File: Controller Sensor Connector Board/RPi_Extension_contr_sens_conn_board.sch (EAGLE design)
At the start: 39 parts, among them J1 22-27-2051-05, J2 22-27-2051-05, X17 53047-03, X18 53047-03, X19 53047-03, X20 53047-03, X21 53047-03, X22 53047-03, X23 53047-03, X24 53047-03, X25 53047-03, X26 53047-03, X27 53047-03, X28 53047-03, X29 53047-03, X30 53047-03, X31 53047-03, X32 53047-03

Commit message: added 40pin connector using 3pin 2row for each muscle
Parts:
- added SV10, SV11, SV12, SV13, SV14, SV15, SV16, SV6, SV7, SV8, SV9: (no value), con-lstb:MA03-2
- added U1: 5103309-8, AMP 5103309-8 40pin:5103309-8
- SV1, SV2, SV3, SV4: device con-lstb:MA08-2 -> con-lstb:MA03-2
- SV5: device con-lstb:MA20-2 -> con-lstb:MA03-2
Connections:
- removed net N$43: X30-1.S
- new net ADC_1: SV1.3
- new net ADC_10: SV10.3
- new net ADC_11: SV11.3
- new net ADC_12: SV12.3
- new net ADC_13: SV13.3
- new net ADC_14: SV14.3
- new net ADC_15: SV15.3
- new net ADC_16: SV16.3
- new net ADC_2: SV2.3
- new net ADC_3: SV3.3
- new net ADC_4: SV4.3
- new net ADC_5: SV5.3
- new net ADC_6: SV6.3
- new net ADC_7: SV7.3
- new net ADC_8: SV8.3
- new net ADC_9: SV9.3, X30-1.S
- new net DAC_1: SV1.1, U1.40
- new net DAC_10: SV10.1, U1.34
- new net DAC_11: SV11.1, U1.30
- new net DAC_12: SV12.1, U1.26
- new net DAC_13: SV13.1, U1.22
- new net DAC_14: SV14.1, U1.18
- new net DAC_15: SV15.1, U1.14
- new net DAC_16: SV16.1, U1.10
- new net DAC_2: SV2.1, U1.36
- new net DAC_3: SV3.1, U1.32
- new net DAC_4: SV4.1, U1.28
- new net DAC_5: SV5.1, U1.24
- new net DAC_6: SV6.1, U1.20
- new net DAC_7: SV7.1, U1.16
- new net DAC_8: SV8.1, U1.12
- new net DAC_9: SV9.1, U1.38
- new net N$100: X1.5
- new net N$101: X5.3
- new net N$102: X5.5
- new net N$103: X9.5
- new net N$104: X9.3
- new net N$105: X2.5
- new net N$106: X2.3
- new net N$107: X6.5
- new net N$108: X6.3
- new net N$109: X10.5
- new net N$11: X11.3
- new net N$110: X10.3
- new net N$111: X16.5
- new net N$112: X16.3
- new net N$12: X11.5
- new net N$14: X7.3
- new net N$15: X7.5
- new net N$17: X3.3
- new net N$18: X3.5
- new net N$2: X13.5
- new net N$20: X4.3
- new net N$21: X4.5
- new net N$23: X8.5
- new net N$24: X8.3
- new net N$26: X12.5
- new net N$27: X12.3
- new net N$3: X13.3
- new net N$5: X14.5
- new net N$6: X14.3
- new net N$67: SV1.6
- new net N$68: SV1.5
- new net N$69: SV5.5
- new net N$70: SV5.6
- new net N$71: SV2.6
- new net N$72: SV2.5
- new net N$73: SV6.6
- new net N$74: SV6.5
- new net N$75: SV9.6
- new net N$76: SV9.5
- new net N$77: SV13.6
- new net N$78: SV13.5
- new net N$79: SV10.6
- new net N$8: X15.3
- new net N$80: SV10.5
- new net N$81: SV14.5
- new net N$82: SV14.6
- new net N$83: SV15.5
- new net N$84: SV15.6
- new net N$85: SV16.6
- new net N$86: SV16.5
- new net N$87: SV12.5
- new net N$88: SV12.6
- new net N$89: SV11.6
- new net N$9: X15.5
- new net N$90: SV11.5
- new net N$91: SV8.5
- new net N$92: SV8.6
- new net N$93: SV4.5
- new net N$94: SV4.6
- new net N$95: SV3.5
- new net N$96: SV3.6
- new net N$97: SV7.5
- new net N$98: SV7.6
- new net N$99: X1.3
- net GND: now also SV1.2, SV1.4, SV10.2, SV10.4, SV11.2, SV11.4, SV12.2, SV12.4, SV13.2, SV13.4, SV14.2, SV14.4, SV15.2, SV15.4, SV16.2, SV16.4, SV2.2, SV2.4, SV3.2, SV3.4, SV4.2, SV4.4, SV5.2, SV5.4, SV6.2, SV6.4, SV7.2, SV7.4, SV8.2, SV8.4, SV9.2, SV9.4, U1.1, U1.11, U1.13, U1.15, U1.17, U1.19, U1.21, U1.23, U1.25, U1.27, U1.29, U1.3, U1.31, U1.33, U1.35, U1.37, U1.39, U1.5, U1.7, U1.9

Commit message: finished first half of connector board
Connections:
- net N$67 renamed LC_P_1
- net N$68 renamed LC_N_1
- removed net N$103: X9.5
- removed net N$104: X9.3
- removed net N$109: X10.5
- removed net N$11: X11.3
- removed net N$110: X10.3
- removed net N$12: X11.5
- removed net N$13: X24-1.S
- removed net N$14: X7.3
- removed net N$15: X7.5
- removed net N$16: X23-1.S
- removed net N$2: X13.5
- removed net N$23: X8.5
- removed net N$24: X8.3
- removed net N$25: X25-1.S
- removed net N$26: X12.5
- removed net N$27: X12.3
- removed net N$28: X26-1.S
- removed net N$3: X13.3
- removed net N$31: X27-1.S
- removed net N$34: X28-1.S
- removed net N$46: X29-1.S
- removed net N$5: X14.5
- removed net N$6: X14.3
- removed net N$75: SV9.6
- removed net N$76: SV9.5
- removed net N$77: SV13.6
- removed net N$78: SV13.5
- removed net N$79: SV10.6
- removed net N$80: SV10.5
- removed net N$81: SV14.5
- removed net N$82: SV14.6
- removed net N$83: SV15.5
- removed net N$84: SV15.6
- removed net N$85: SV16.6
- removed net N$86: SV16.5
- removed net N$87: SV12.5
- removed net N$88: SV12.6
- removed net N$89: SV11.6
- removed net N$90: SV11.5
- new net LC_N_10: SV10.5, X13.3
- new net LC_N_11: SV11.5, X12.3
- new net LC_N_12: SV12.5, X11.3
- new net LC_N_13: SV13.5, X10.3
- new net LC_N_14: SV14.5, X9.3
- new net LC_N_15: SV15.5, X8.3
- new net LC_N_16: SV16.5, X7.3
- new net LC_N_9: SV9.5, X14.3
- new net LC_P_10: SV10.6, X13.5
- new net LC_P_11: SV11.6, X12.5
- new net LC_P_12: SV12.6, X11.5
- new net LC_P_13: SV13.6, X10.5
- new net LC_P_14: SV14.6, X9.5
- new net LC_P_15: SV15.6, X8.5
- new net LC_P_16: SV16.6, X7.5
- new net LC_P_9: SV9.6, X14.5
- net ADC_10: now also X29-1.S
- net ADC_11: now also X28-1.S
- net ADC_12: now also X27-1.S
- net ADC_13: now also X26-1.S
- net ADC_14: now also X25-1.S
- net ADC_15: now also X24-1.S
- net ADC_16: now also X23-1.S
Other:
- moved on the sheet: SV1, SV10, SV11, SV13, SV14, SV15, SV2, SV3, SV5, SV6, SV7, SV9

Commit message: finished second half of connector board
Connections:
- removed net N$1: X17-1.S
- removed net N$10: X20-1.S
- removed net N$100: X1.5
- removed net N$101: X5.3
- removed net N$102: X5.5
- removed net N$105: X2.5
- removed net N$106: X2.3
- removed net N$107: X6.5
- removed net N$108: X6.3
- removed net N$111: X16.5
- removed net N$112: X16.3
- removed net N$17: X3.3
- removed net N$18: X3.5
- removed net N$19: X22-1.S
- removed net N$20: X4.3
- removed net N$21: X4.5
- removed net N$22: X21-1.S
- removed net N$37: X32-1.S
- removed net N$4: X18-1.S
- removed net N$40: X31-1.S
- removed net N$69: SV5.5
- removed net N$7: X19-1.S
- removed net N$70: SV5.6
- removed net N$71: SV2.6
- removed net N$72: SV2.5
- removed net N$73: SV6.6
- removed net N$74: SV6.5
- removed net N$8: X15.3
- removed net N$9: X15.5
- removed net N$91: SV8.5
- removed net N$92: SV8.6
- removed net N$93: SV4.5
- removed net N$94: SV4.6
- removed net N$95: SV3.5
- removed net N$96: SV3.6
- removed net N$97: SV7.5
- removed net N$98: SV7.6
- removed net N$99: X1.3
- new net LC_N_2: SV2.5, X16.3
- new net LC_N_3: SV3.5, X1.3
- new net LC_N_4: SV4.5, X2.3
- new net LC_N_5: SV5.5, X3.3
- new net LC_N_6: SV6.5, X4.3
- new net LC_N_7: SV7.5, X5.3
- new net LC_N_8: SV8.5, X6.3
- new net LC_P_2: SV2.6, X16.5
- new net LC_P_3: SV3.6, X1.5
- new net LC_P_4: SV4.6, X2.5
- new net LC_P_5: SV5.6, X3.5
- new net LC_P_6: SV6.6, X4.5
- new net LC_P_7: SV7.6, X5.5
- new net LC_P_8: SV8.6, X6.5
- net ADC_1: now also X31-1.S
- net ADC_2: now also X32-1.S
- net ADC_3: now also X17-1.S
- net ADC_4: now also X18-1.S
- net ADC_5: now also X19-1.S
- net ADC_6: now also X20-1.S
- net ADC_7: now also X21-1.S
- net ADC_8: now also X22-1.S
- net LC_N_1: now also X15.3
- net LC_P_1: now also X15.5
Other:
- moved on the sheet: J1-1, J1-2, J1-3, J1-4, J1-5, J2-1, J2-2, J2-3, J2-4, J2-5, SV1, SV10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

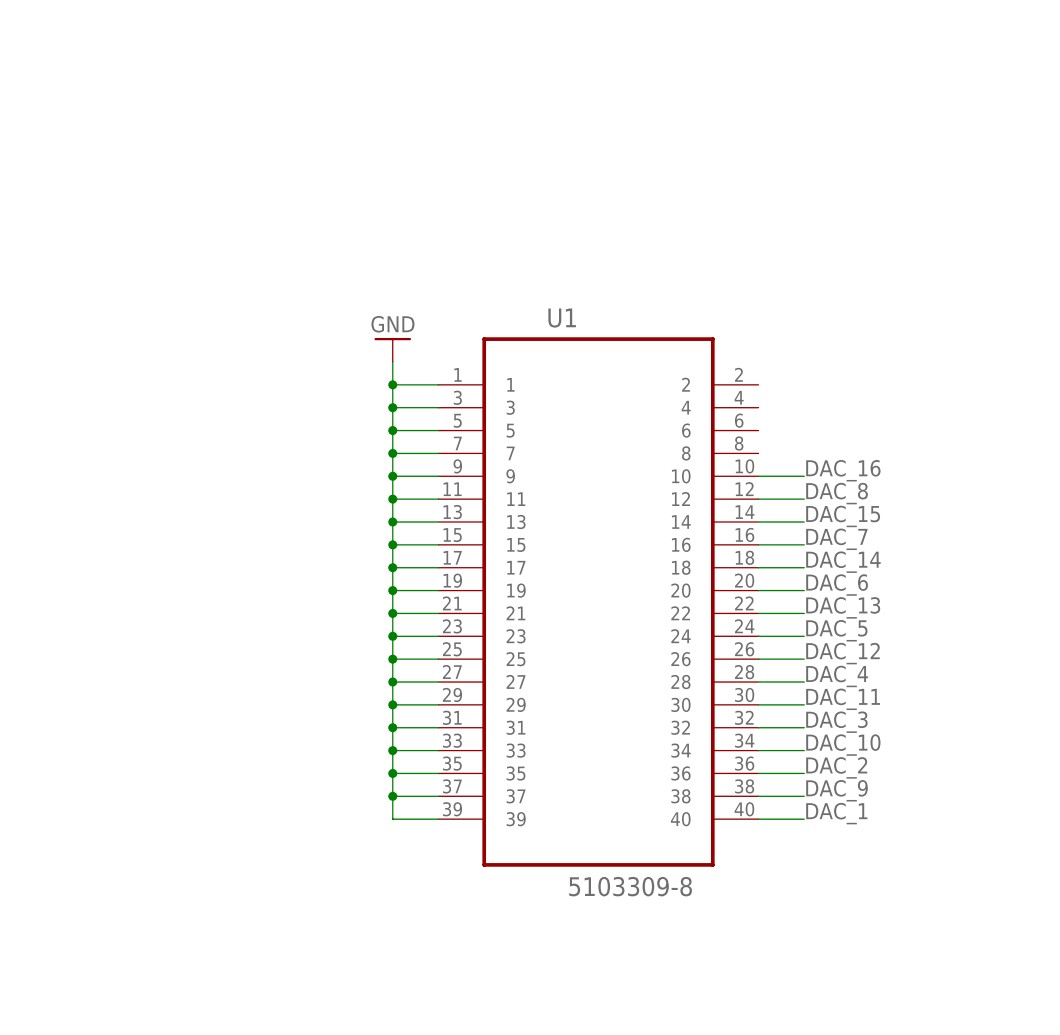
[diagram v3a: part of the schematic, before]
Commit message: adjusted silkscreen
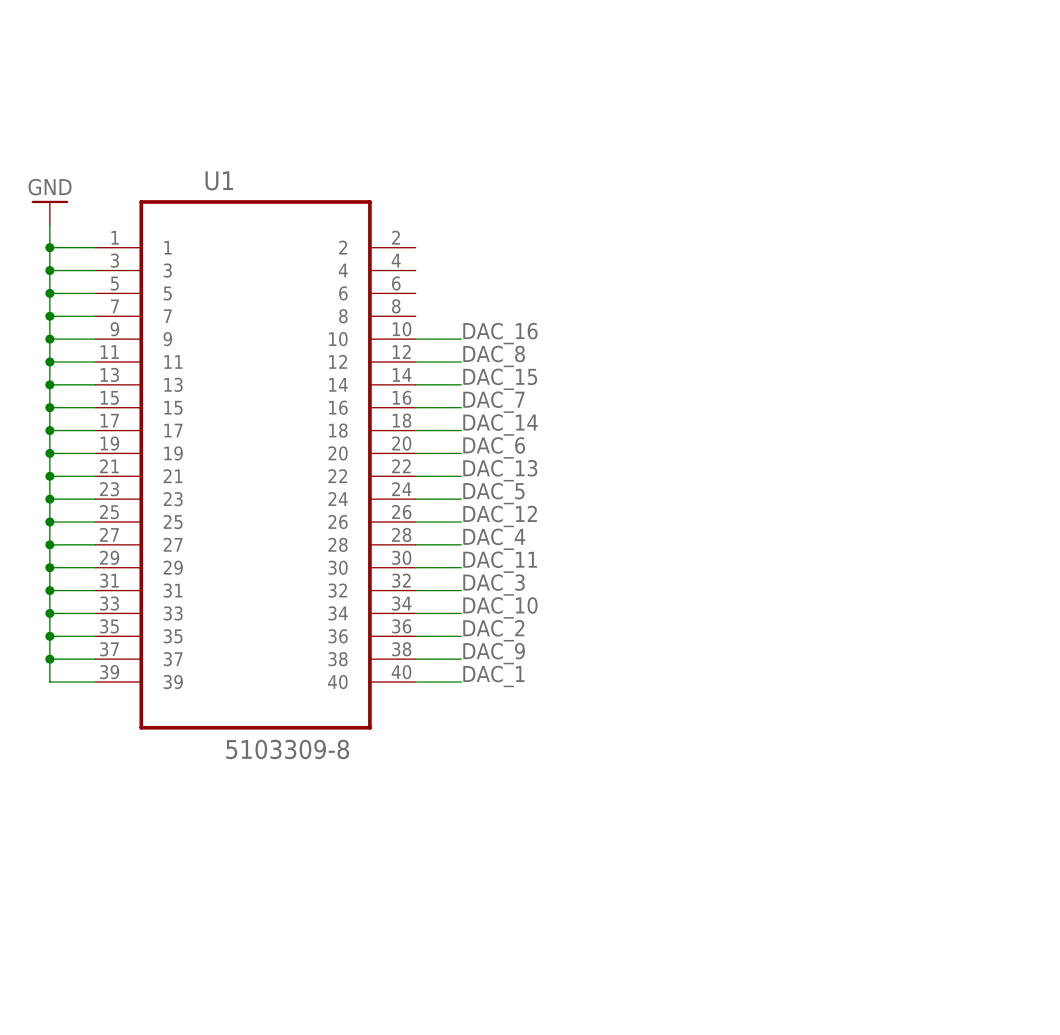
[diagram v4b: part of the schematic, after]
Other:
- moved on the sheet: U1

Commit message: changed dac header to 34pin
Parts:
- U1: value 5103309-8 -> 5103309-7; device AMP 5103309-8 40pin:5103309-8 -> AMP 5103309-7 34pin:5103309-7
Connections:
- net DAC_1: now also U1.1; no longer U1.40
- net DAC_10: now also U1.7; no longer U1.34
- net DAC_11: now also U1.11; no longer U1.30
- net DAC_12: now also U1.15; no longer U1.26
- net DAC_13: now also U1.19; no longer U1.22
- net DAC_14: now also U1.23; no longer U1.18
- net DAC_15: now also U1.27; no longer U1.14
- net DAC_16: now also U1.31; no longer U1.10
- net DAC_2: now also U1.5; no longer U1.36
- net DAC_3: now also U1.9; no longer U1.32
- net DAC_4: now also U1.13; no longer U1.28
- net DAC_5: now also U1.17; no longer U1.24
- net DAC_6: now also U1.21; no longer U1.20
- net DAC_7: now also U1.25; no longer U1.16
- net DAC_8: now also U1.29; no longer U1.12
- net DAC_9: now also U1.3; no longer U1.38
- net GND: now also U1.10, U1.12, U1.14, U1.16, U1.18, U1.2, U1.20, U1.22, U1.24, U1.26, U1.28, U1.30, U1.32, U1.34, U1.4, U1.6, U1.8; no longer U1.1, U1.11, U1.13, U1.15, U1.17, U1.19, U1.21, U1.23, U1.25, U1.27, U1.29, U1.3, U1.31, U1.33, U1.35, U1.37, U1.39, U1.5, U1.7, U1.9
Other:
- moved on the sheet: SV1, SV10, SV11, SV12, SV13, SV14, SV15, SV16, SV2, SV3, SV4, SV5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
